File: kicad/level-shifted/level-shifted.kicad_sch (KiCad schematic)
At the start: 27 parts, among them J101 Conn_01x09_Socket, J102 Conn_01x09_Socket, J103 Conn_01x09_Socket, J104 PAL-1 Expansion Connector, J105 Conn_01x09_Socket, J106 Conn_01x09_Socket, J107 Conn_01x09_Socket, J109 Conn_01x09_Socket, J110 Conn_01x09_Socket, SW101 PICO RESET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

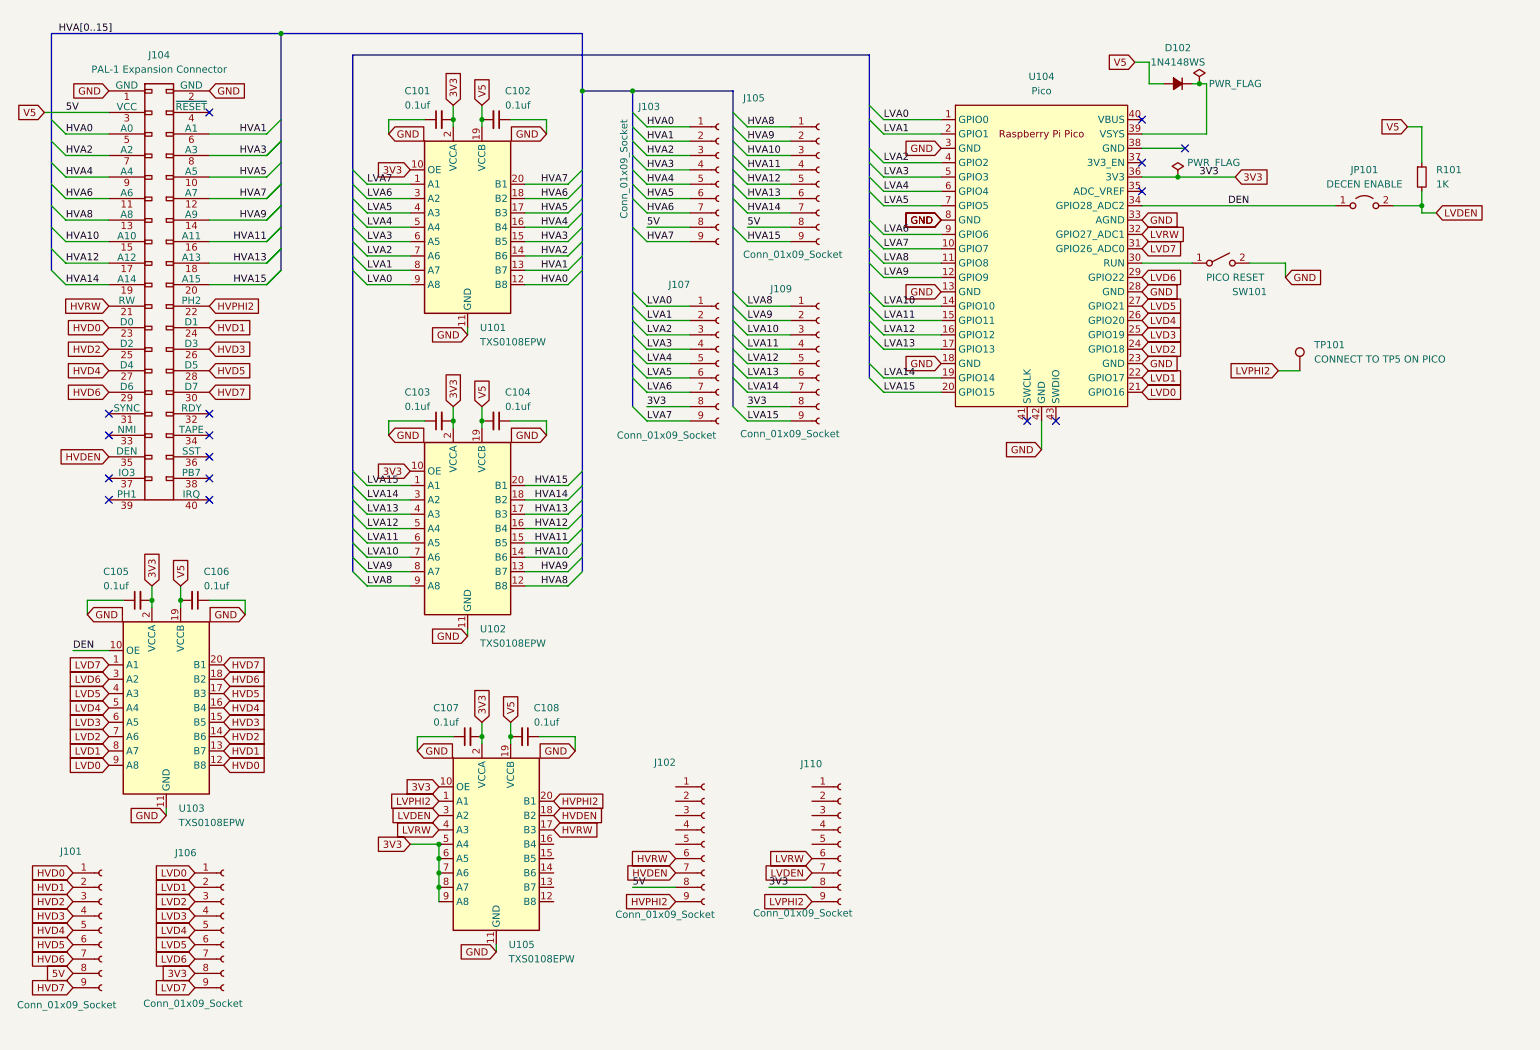
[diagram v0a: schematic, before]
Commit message: PCB for the level shifted version
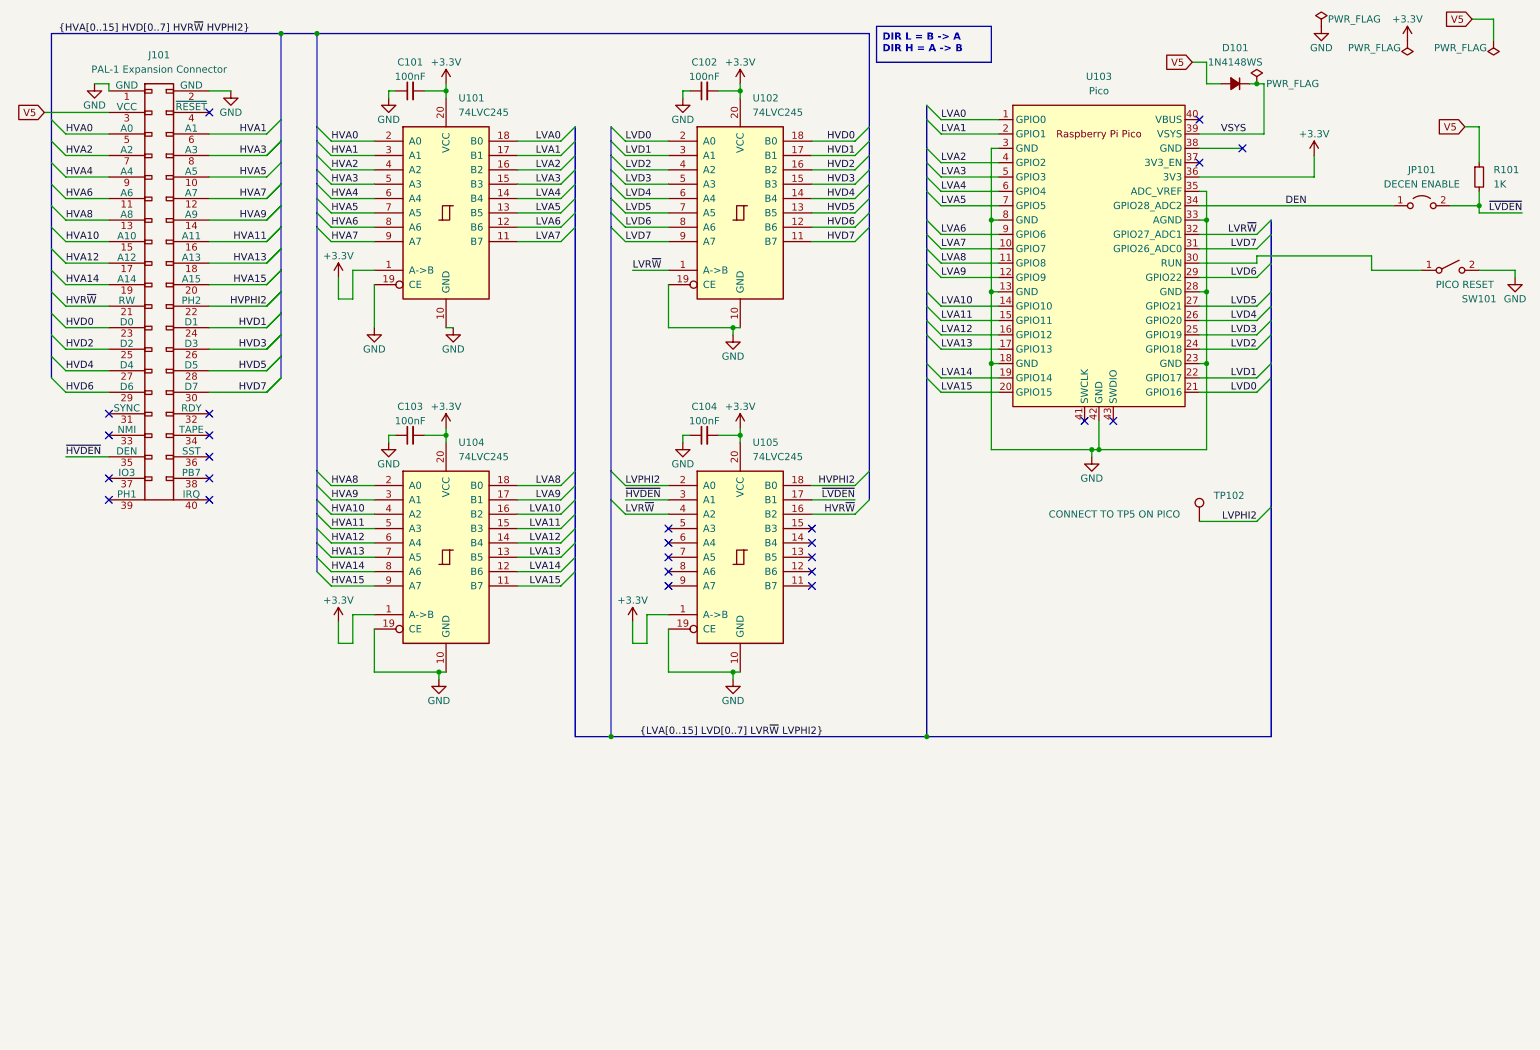
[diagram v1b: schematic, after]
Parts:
- removed C105, C106, C107, C108: 0.1uf, Capacitor_SMD:C_0603_1608Metric_Pad1.08x0.95mm_HandSolder, symbol Device:C_Small
- removed J101, J102, J103, J105, J106, J107, J109, J110: Conn_01x09_Socket, Connector_PinHeader_1.27mm:PinHeader_1x09_P1.27mm_Vertical, symbol Connector:Conn_01x09_Socket
- removed TP101: CONNECT TO TP5 ON PICO, TestPoint:TestPoint_Pad_2.5x2.5mm, symbol Connector:TestPoint
- removed U101, U102, U103, U105: TXS0108EPW, Package_SO:TSSOP-20_4.4x6.5mm_P0.65mm, symbol Logic_LevelTranslator:TXS0108EPW
- added TP102: CONNECT TO TP5 ON PICO, TestPoint:TestPoint_Pad_2.5x2.5mm, symbol Connector:TestPoint
- added U101, U102, U104, U105: 74LVC245, Package_DIP:DIP-20_W7.62mm_Socket_LongPads, symbol 74xx:74LS245
- C101, C102, C103, C104: value 0.1uf -> 100nF; footprint Capacitor_SMD:C_0603_1608Metric_Pad1.08x0.95mm_HandSolder -> Capacitor_THT:C_Disc_D4.7mm_W2.5mm_P5.00mm
- D101: renamed from D102; footprint Diode_SMD:D_SOD-323F -> Diode_THT:D_A-405_P7.62mm_Horizontal
- JP101: footprint Jumper:SolderJumper-2_P1.3mm_Open_RoundedPad1.0x1.5mm -> Connector_PinHeader_2.54mm:PinHeader_1x02_P2.54mm_Vertical
- R101: footprint Resistor_SMD:R_0603_1608Metric_Pad0.98x0.95mm_HandSolder -> Resistor_THT:R_Axial_DIN0204_L3.6mm_D1.6mm_P5.08mm_Horizontal
- SW101: footprint Button_Switch_SMD:SW_Push_1P1T_XKB_TS-1187A -> Button_Switch_THT:SW_PUSH_6mm_H4.3mm
- renumbered J104 to J101, U104 to U103
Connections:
- net GND: now also U103.35 (ADC_VREF), U101.10 (GND), U101.19 (CE), U102.10 (GND), U102.19 (CE), U104.10 (GND), U104.19 (CE), U105.10 (GND), U105.19 (CE)
- net HVA0: now also U101.2 (A0)
- net HVA1: now also U101.3 (A1)
- net HVA10: now also U104.4 (A2)
- net HVA11: now also U104.5 (A3)
- net HVA12: now also U104.6 (A4)
- net HVA13: now also U104.7 (A5)
- net HVA14: now also U104.8 (A6)
- net HVA15: now also U104.9 (A7)
- net HVA2: now also U101.4 (A2)
- net HVA3: now also U101.5 (A3)
- net HVA4: now also U101.6 (A4)
- net HVA5: now also U101.7 (A5)
- net HVA6: now also U101.8 (A6)
- net HVA7: now also U101.9 (A7)
- net HVA8: now also U104.2 (A0)
- net HVA9: now also U104.3 (A1)
- net HVD0: now also U102.18 (B0)
- net HVD1: now also U102.17 (B1)
- net HVD2: now also U102.16 (B2)
- net HVD3: now also U102.15 (B3)
- net HVD4: now also U102.14 (B4)
- net HVD5: now also U102.13 (B5)
- net HVD6: now also U102.12 (B6)
- net HVD7: now also U102.11 (B7)
- net HVPHI2: now also U105.18 (B0)
- net LVA0: now also U101.18 (B0)
- net LVA1: now also U101.17 (B1)
- net LVA10: now also U104.16 (B2)
- net LVA11: now also U104.15 (B3)
- net LVA12: now also U104.14 (B4)
- net LVA13: now also U104.13 (B5)
- net LVA14: now also U104.12 (B6)
- net LVA15: now also U104.11 (B7)
- net LVA2: now also U101.16 (B2)
- net LVA3: now also U101.15 (B3)
- net LVA4: now also U101.14 (B4)
- net LVA5: now also U101.13 (B5)
- net LVA6: now also U101.12 (B6)
- net LVA7: now also U101.11 (B7)
- net LVA8: now also U104.18 (B0)
- net LVA9: now also U104.17 (B1)
- net LVD0: now also U102.2 (A0)
- net LVD1: now also U102.3 (A1)
- net LVD2: now also U102.4 (A2)
- net LVD3: now also U102.5 (A3)
- net LVD4: now also U102.6 (A4)
- net LVD5: now also U102.7 (A5)
- net LVD6: now also U102.8 (A6)
- net LVD7: now also U102.9 (A7)
- net LVPHI2: now also TP102.1, U105.2 (A0)
- net VSYS: now reaches D101.1 (K), U103.39 (VSYS)
- net 3V3 renamed +3.3V
- net +3.3V: now also C102.2, C104.2, U101.1 (A->B), U101.20 (VCC), U102.20 (VCC), U104.1 (A->B), U104.20 (VCC), U105.1 (A->B), U105.20 (VCC)
- net 5V renamed V5
- net V5: no longer C102.2, C104.2
- net HVDEN renamed ~{HVDEN}
- net ~{HVDEN}: now also U105.3 (A1)
- net HVRW renamed HVR~{W}
- net HVR~{W}: now also U105.16 (B2)
- net LVDEN renamed ~{LVDEN}
- net ~{LVDEN}: now also U105.17 (B1)
- net LVRW renamed LVR~{W}
- net LVR~{W}: now also U102.1 (A->B), U105.4 (A2)
- no-connect marks 16 -> 25
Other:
- moved on the sheet: D101, JP101, R101, SW101, U103

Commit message: Trial of multiplexed code
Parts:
- removed R101: 1K, Resistor_THT:R_Axial_DIN0204_L3.6mm_D1.6mm_P5.08mm_Horizontal, symbol Device:R_Small
- removed TP102: CONNECT TO TP5 ON PICO, TestPoint:TestPoint_Pad_2.5x2.5mm, symbol Connector:TestPoint
- added C105: 100nF, Capacitor_SMD:C_1812_4532Metric_Pad1.57x3.40mm_HandSolder, symbol Device:C_Small
- added J102: PAL-1 Expansion Connector, Connector_PinHeader_2.54mm:PinHeader_2x20_P2.54mm_Vertical, symbol pal1:Expansion_Connector
- added TP101: CONNECT TO TP5 ON PICO, TestPoint:TestPoint_Pad_2.5x2.5mm, symbol Connector:TestPoint
- added U106: 74LS00, Package_DIP:DIP-14_W8.89mm_SMDSocket_LongPads, symbol 74xx:74LS00
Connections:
- net +3.3V: no longer U105.1 (A->B)
- net GND: now also U105.1 (A->B), C105.1, J102.1 (GND), J102.2 (GND), U106.10, U106.7 (GND), U106.9; no longer U102.19 (CE)
- net HVA0: now also J102.5 (A0)
- net HVA1: now also J102.6 (A1)
- net HVA10: now also J102.15 (A10)
- net HVA11: now also J102.16 (A11)
- net HVA12: now also J102.17 (A12)
- net HVA13: now also J102.18 (A13)
- net HVA14: now also J102.19 (A14)
- net HVA15: now also J102.20 (A15)
- net HVA2: now also J102.7 (A2)
- net HVA3: now also J102.8 (A3)
- net HVA4: now also J102.9 (A4)
- net HVA5: now also J102.10 (A5)
- net HVA6: now also J102.11 (A6)
- net HVA7: now also J102.12 (A7)
- net HVA8: now also J102.13 (A8)
- net HVA9: now also J102.14 (A9)
- net HVD0: now also J102.23 (D0)
- net HVD1: now also J102.24 (D1)
- net HVD2: now also J102.25 (D2)
- net HVD3: now also J102.26 (D3)
- net HVD4: now also J102.27 (D4)
- net HVD5: now also J102.28 (D5)
- net HVD6: now also J102.29 (D6)
- net HVD7: now also J102.30 (D7)
- net HVPHI2: now also J102.22 (PH2), TP101.1, U106.5
- net HVR~{W}: now also J102.21 (RW), U106.1, U106.2
- net V5: now also C105.2, J102.3 (VCC), U106.14 (VCC)
- net ~{HVDEN}: now also JP101.2 (B), J102.35 (DEN); no longer U105.3 (A1)
- net ~{LVDEN}: now also U103.34 (GPIO28_ADC2), U106.12, U106.13; no longer JP101.2 (B)
- net ~{HV_W}: now reaches U105.15 (B3)
- net ~{HV_W}: now also U102.1 (A->B), U106.6
- net ~{LV_W}: now reaches U105.5 (A3)
- net ~{LV_W}: now also U103.32 (GPIO27_ADC1)
- net DEN renamed ~{DEN_S}
- net ~{DEN_S}: now also U105.3 (A1); no longer U103.34 (GPIO28_ADC2)
- net LVPHI2: no longer names the net of U105.2 (A0)
- removed net LVR~{W}: U102.1 (A->B), U103.32 (GPIO27_ADC1), U105.4 (A2)
- new net DATA_EN: U102.19 (CE), U106.11
- new net ~{R}W: U106.3, U106.4
- no-connect marks 25 -> 36
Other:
- moved on the sheet: JP101, SW101
